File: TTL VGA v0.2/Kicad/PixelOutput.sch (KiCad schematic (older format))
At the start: 5 parts, among them U19 GAL16V8

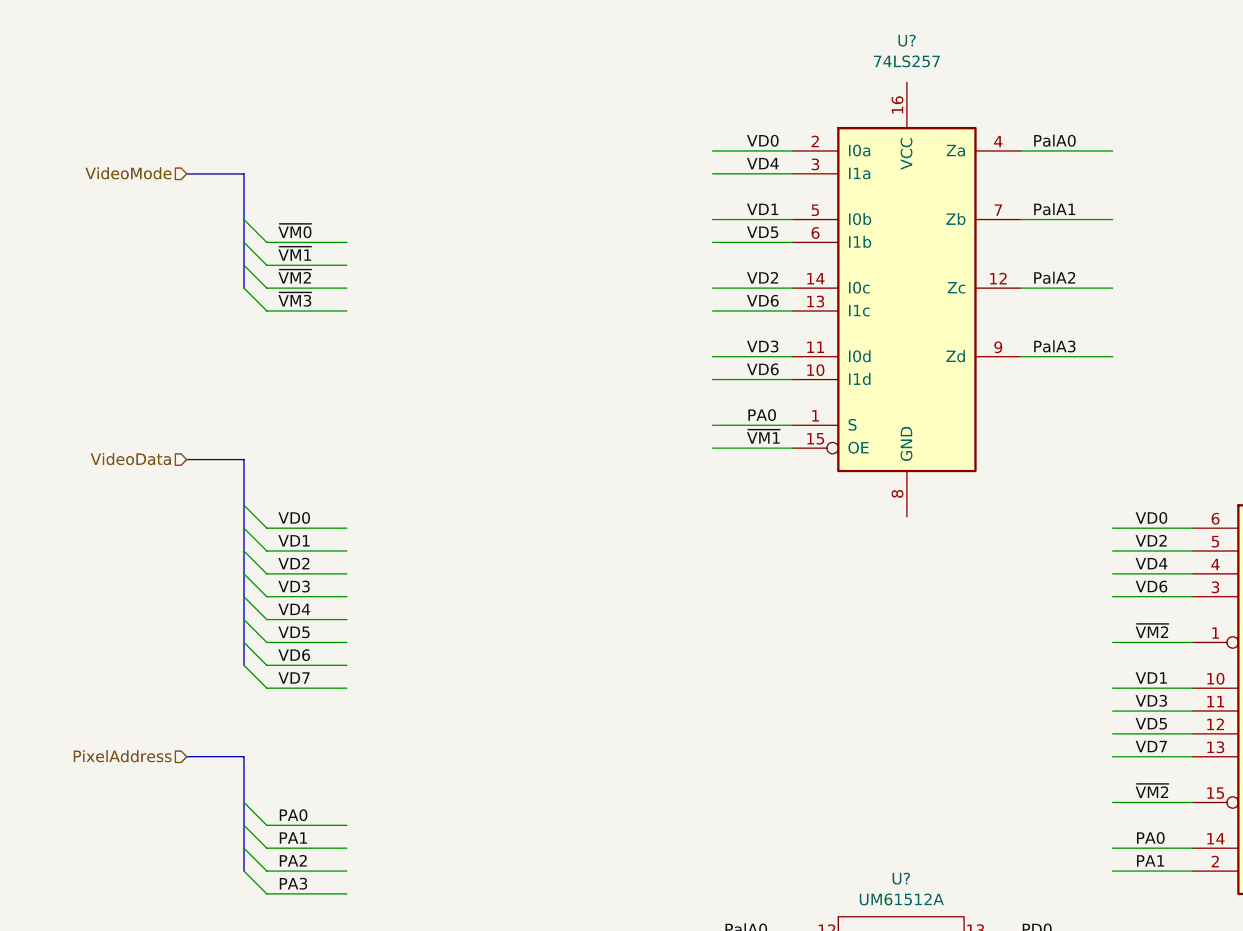
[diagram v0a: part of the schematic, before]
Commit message: video bit mux
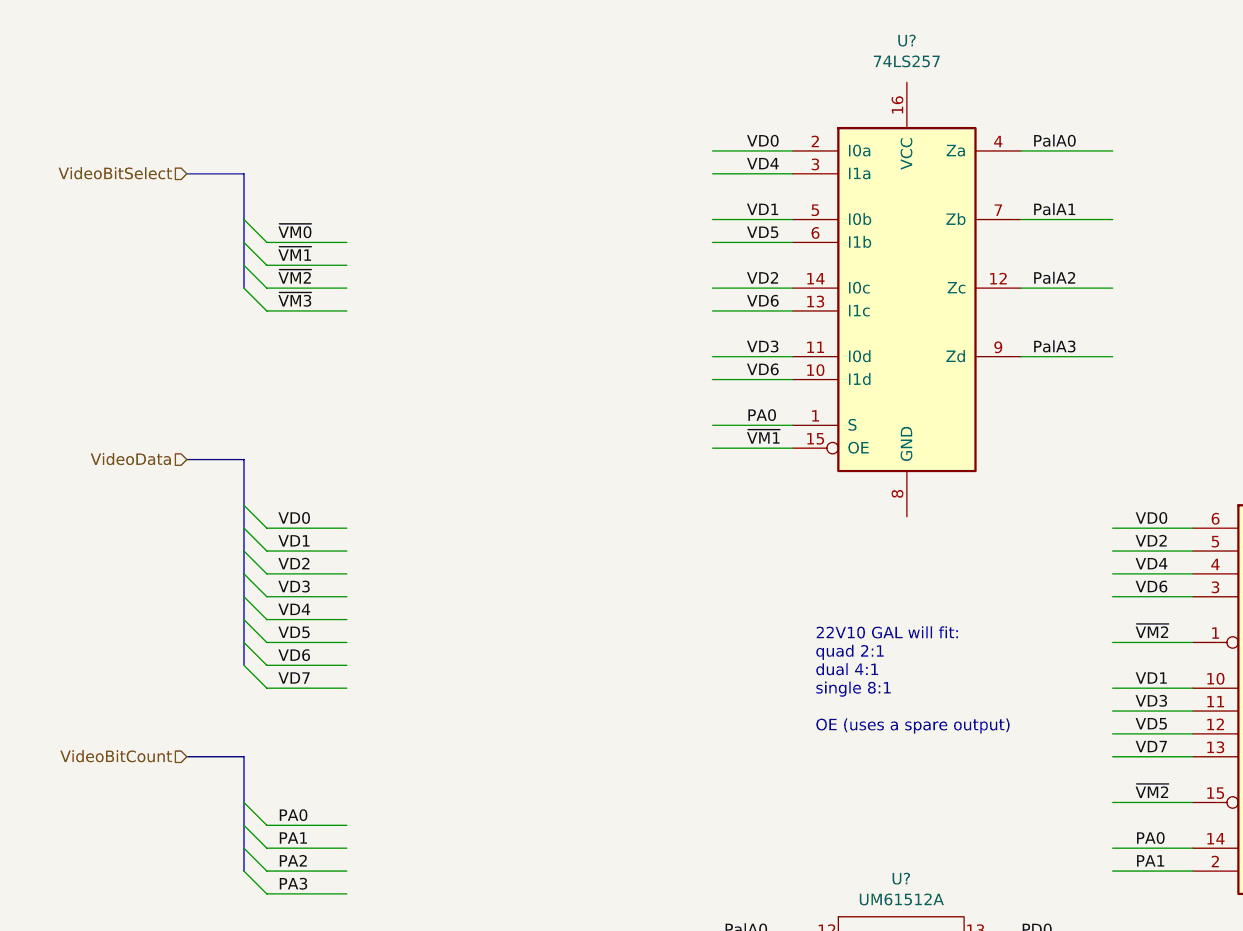
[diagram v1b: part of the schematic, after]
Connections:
- net labels added: VideoBitCount, VideoBitSelect
- net labels removed: PixelAddress, VideoMode
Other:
- note added: "22V10 GAL will fit:\nquad 2:1\ndual 4:1\nsingle 8:1\n\nOE (uses a spare output)"
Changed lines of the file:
@@
 $EndComp
 Text HLabel 1450 1650 0    50   Input ~ 0
-VideoMode
+VideoBitSelect
 Text HLabel 1450 4200 0    50   Input ~ 0
-PixelAddress
+VideoBitCount
 Text Notes 4200 7450 0    50   ~ 0
           VD0  VD1  VD2  VD3  VD4  VD5  VD6  VD7\nVM1: | PA = 0                   | PA = 1                    \nVM2: | PA = 0   | PA =1    | PA = 2    | PA = 3\nVM3: | PA0  | PA1 | PA2 | PA3 | PA4 | PA5 | PA6 | PA7\n
@@
 Wire Wire Line
 	4950 5000 5300 5000
-Wire Bus Line
-	1700 1650 1700 2150
-Wire Bus Line
-	1700 4200 1700 4700
-Wire Bus Line
-	1700 2900 1700 3800
 Wire Wire Line
 	4950 5100 5300 5100
@@
 Text Label 5100 5700 0    50   ~ 0
 PD7
+Wire Bus Line
+	1700 1650 1700 2150
+Wire Bus Line
+	1700 4200 1700 4700
+Wire Bus Line
+	1700 2900 1700 3800
+Text Notes 4200 4100 0    50   ~ 0
+22V10 GAL will fit:\nquad 2:1\ndual 4:1\nsingle 8:1\n\nOE (uses a spare output)
 $EndSCHEMATC

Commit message: update kicad
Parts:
- added U?: 74HCT574, symbol 74xx:74HCT574
- added U?: 74LS245, symbol 74xx:74LS245
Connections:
- net labels added: BD0, BD1, BD2, BD3, BD4, BD5, BD6, BD7, BusData, ColorDepthSelect, PalA10, PalA11, PalA7, PalA8, PalA9, PaletteRegStrobe, ~1bit, ~2bit, ~4bit, ~8bit, ~CDS0, ~CDS1, ~CDS2
- net labels removed: VideoBitSelect, ~VM0, ~VM1, ~VM2, ~VM3
- wire segments 99 -> 132
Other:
- note added: "8-bit color depth will bypass the Palette.\nIf we have 8-bit colors.\nIf we choose 15/16-bit colors we need to map."
- note added: "Have a Register that selects the Palette\nto switch quickly between presets.\nOnly if not 8-bit color depth.\nStobe allowed mid-frame."
- note removed: "VD0 VD1 VD2 VD3 VD4 VD5 VD6 VD7\nVM1: | PA = 0 | PA = 1 \nVM2: | PA = 0 | PA =1 | PA = 2 | PA = 3\nVM3: | PA0 | PA1 | PA2 | PA3 | PA4 | PA5 | PA6 | PA7\n"
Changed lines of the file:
@@
 Wire Wire Line
 	9800 2000 10600 2000
-Wire Wire Line
-	9800 2100 10050 2100
-Wire Wire Line
-	9800 2200 10600 2200
 Text Label 10400 1500 0    50   ~ 0
 R0
@@
 B2
 Wire Wire Line
-	10050 2100 10050 2300
-Connection ~ 10050 2100
-Wire Wire Line
-	10050 2100 10600 2100
-Wire Wire Line
 	10050 2300 10600 2300
 Text Notes 9050 950  0    50   ~ 0
@@
 $EndComp
 Text HLabel 1450 1650 0    50   Input ~ 0
-VideoBitSelect
+ColorDepthSelect
 Text HLabel 1450 4200 0    50   Input ~ 0
 VideoBitCount
-Text Notes 4200 7450 0    50   ~ 0
-          VD0  VD1  VD2  VD3  VD4  VD5  VD6  VD7\nVM1: | PA = 0                   | PA = 1                    \nVM2: | PA = 0   | PA =1    | PA = 2    | PA = 3\nVM3: | PA0  | PA1 | PA2 | PA3 | PA4 | PA5 | PA6 | PA7\n
 $Comp
 L 74xx:74LS251 U?
@@
 	7550 5800 7200 5800
 Text Label 7350 5800 0    50   ~ 0
-~VM3
+~1bit
 $Comp
 L 74xx:74LS253 U?
@@
 VD7
 Text Label 5600 3700 0    50   ~ 0
-~VM2
+~2bit
 Text Label 5600 4400 0    50   ~ 0
-~VM2
+~2bit
 Text Label 5600 4600 0    50   ~ 0
 PA0
@@
 PalA3
 Text Label 3900 2850 0    50   ~ 0
-~VM1
+~4bit
 Text Label 3900 2750 0    50   ~ 0
 PA0
@@
 Entry Wire Line
 	1700 2050 1800 2150
-Entry Wire Line
-	1700 2150 1800 2250
 Wire Bus Line
 	1700 1650 1450 1650
-Wire Wire Line
-	1800 1950 2150 1950
-Wire Wire Line
-	1800 2050 2150 2050
-Wire Wire Line
-	1800 2150 2150 2150
-Wire Wire Line
-	1800 2250 2150 2250
 Text Label 1850 1950 0    50   ~ 0
-~VM0
+~CDS0
 Text Label 1850 2050 0    50   ~ 0
-~VM1
+~CDS1
 Text Label 1850 2150 0    50   ~ 0
-~VM2
-Text Label 1850 2250 0    50   ~ 0
-~VM3
+~CDS2
 Text Notes 4350 6750 0    50   ~ 0
 Palette RAM
@@
 Text Label 5100 5700 0    50   ~ 0
 PD7
-Wire Bus Line
-	1700 1650 1700 2150
-Wire Bus Line
-	1700 4200 1700 4700
-Wire Bus Line
-	1700 2900 1700 3800
 Text Notes 4200 4100 0    50   ~ 0
 22V10 GAL will fit:\nquad 2:1\ndual 4:1\nsingle 8:1\n\nOE (uses a spare output)
+Wire Wire Line
+	4200 5700 3750 5700
+Wire Wire Line
+	4200 5800 3750 5800
+Text Label 3800 5700 0    50   ~ 0
+PalA7
+Wire Wire Line
+	4200 5900 3750 5900
+Wire Wire Line
+	4200 6000 3750 6000
+Wire Wire Line
+	4200 6100 3750 6100
+Text Notes 950  7200 0    50   ~ 0
+Have a Register that selects the Palette\nto switch quickly between presets.\nOnly if not 8-bit color depth.\nStobe allowed mid-frame.
+Text Notes 5250 6300 0    50   ~ 0
+8-bit color depth will bypass the Palette.\nIf we have 8-bit colors.\nIf we choose 15/16-bit colors we need to map.
+$Comp
+L 74xx:74HCT574 U?
+U 1 1 5EBE347D
+P 1900 6050
+F 0 "U?" H 1900 7031 50  0000 C CNN
+F 1 "74HCT574" H 1900 6940 50  0000 C CNN
+F 2 "" H 1900 6050 50  0001 C CNN
+F 3 "http://www.ti.com/lit/gpn/sn74HCT574" H 1900 6050 50  0001 C CNN
+	1    1900 6050
+	1    0    0    -1
+$EndComp
+Wire Wire Line
+	1400 5550 1050 5550
+Wire Wire Line
+	1400 5650 1050 5650
+Wire Wire Line
+	1400 5750 1050 5750
+Wire Wire Line
+	1400 5850 1050 5850
+Wire Wire Line
+	1400 5950 1050 5950
+Wire Wire Line
+	1400 6050 1050 6050
+Wire Wire Line
+	1400 6150 1050 6150
+Wire Wire Line
+	1400 6250 1050 6250
+Entry Wire Line
+	950  5450 1050 5550
+Entry Wire Line
+	950  5550 1050 5650
+Entry Wire Line
+	950  5650 1050 5750
+Entry Wire Line
+	950  5750 1050 5850
+Entry Wire Line
+	950  5850 1050 5950
+Entry Wire Line
+	950  5950 1050 6050
+Entry Wire Line
+	950  6050 1050 6150
+Entry Wire Line
+	950  6150 1050 6250
+Wire Bus Line
+	950  5350 850  5350
+Text HLabel 850  5350 0    50   Input ~ 0
+BusData
+Text HLabel 1200 6450 0    50   Input ~ 0
+PaletteRegStrobe
+Wire Wire Line
+	1200 6450 1400 6450
+Text Label 1100 5550 0    50   ~ 0
+BD0
+Text Label 1100 5650 0    50   ~ 0
+BD1
+Text Label 1100 5750 0    50   ~ 0
+BD2
+Text Label 1100 5850 0    50   ~ 0
+BD3
+Text Label 1100 5950 0    50   ~ 0
+BD4
+Text Label 1100 6050 0    50   ~ 0
+BD5
+Text Label 1100 6150 0    50   ~ 0
+BD6
+Text Label 1100 6250 0    50   ~ 0
+BD7
+Wire Wire Line
+	2400 5550 2800 5550
+Wire Wire Line
+	2400 5650 2800 5650
+Wire Wire Line
+	2400 5750 2800 5750
+Wire Wire Line
+	2400 5850 2800 5850
+Wire Wire Line
+	2400 5950 2800 5950
+Wire Wire Line
+	2400 6050 2800 6050
+Wire Wire Line
+	2400 6150 2800 6150
+Wire Wire Line
+	2400 6250 2800 6250
+Text Label 2500 5550 0    50   ~ 0
+PalA4
+Text Label 2500 5650 0    50   ~ 0
+PalA5
+Text Label 2500 5750 0    50   ~ 0
+PalA6
+Text Label 2500 5850 0    50   ~ 0
+PalA7
+Text Label 2500 5950 0    50   ~ 0
+PalA8
+Text Label 2500 6050 0    50   ~ 0
+PalA9
+Text Label 2500 6150 0    50   ~ 0
+PalA10
+Text Label 2500 6250 0    50   ~ 0
+PalA11
+Text Label 3800 5800 0    50   ~ 0
+PalA8
+Text Label 3800 5900 0    50   ~ 0
+PalA9
+Text Label 3800 6000 0    50   ~ 0
+PalA10
+Text Label 3800 6100 0    50   ~ 0
+PalA11
+$Comp
+L 74xx:74LS245 U?
+U 1 1 5EC04F82
+P 2650 3700
+F 0 "U?" H 2650 4681 50  0000 C CNN
+F 1 "74LS245" H 2650 4590 50  0000 C CNN
+F 2 "" H 2650 3700 50  0001 C CNN
+F 3 "http://www.ti.com/lit/gpn/sn74LS245" H 2650 3700 50  0001 C CNN
+	1    2650 3700
+	1    0    0    -1
+$EndComp
+Wire Wire Line
+	3150 3200 3450 3200
+Wire Wire Line
+	3150 3300 3450 3300
+Wire Wire Line
+	3150 3400 3450 3400
+Wire Wire Line
+	3150 3500 3450 3500
+Wire Wire Line
+	3150 3600 3450 3600
+Wire Wire Line
+	3150 3700 3450 3700
+Wire Wire Line
+	3150 3800 3450 3800
+Wire Wire Line
+	3150 3900 3450 3900
+Text Label 3250 3200 0    50   ~ 0
+PD0
+Text Label 3250 3300 0    50   ~ 0
+PD1
+Text Label 3250 3400 0    50   ~ 0
+PD2
+Text Label 3250 3500 0    50   ~ 0
+PD3
+Text Label 3250 3600 0    50   ~ 0
+PD4
+Text Label 3250 3700 0    50   ~ 0
+PD5
+Text Label 3250 3800 0    50   ~ 0
+PD6
+Text Label 3250 3900 0    50   ~ 0
+PD7
+Wire Wire Line
+	2150 4200 1850 4200
+Text Label 1900 4200 0    50   ~ 0
+~8bit
+Wire Wire Line
+	9800 2100 10150 2100
+Wire Wire Line
+	9800 2200 10050 2200
+Wire Wire Line
+	10050 2200 10050 2300
+Wire Wire Line
+	10600 2200 10150 2200
+Wire Wire Line
+	10150 2200 10150 2100
+Connection ~ 10150 2100
+Wire Wire Line
+	10150 2100 10600 2100
+Wire Wire Line
+	1800 1950 2650 1950
+Wire Wire Line
+	1800 2050 2650 2050
+Wire Wire Line
+	1800 2150 2650 2150
+Text Label 2450 1950 0    50   ~ 0
+~1bit
+Text Label 2450 2050 0    50   ~ 0
+~2bit
+Text Label 2450 2150 0    50   ~ 0
+~4bit
+Wire Wire Line
+	1800 2300 2650 2300
+Wire Bus Line
+	1700 1650 1700 2050
+Wire Bus Line
+	1700 4200 1700 4700
+Wire Bus Line
+	950  5350 950  6150
+Wire Bus Line
+	1700 2900 1700 3800
+Text Label 2450 2300 0    50   ~ 0
+~8bit
 $EndSCHEMATC

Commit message: Update
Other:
- note added: "22V10 GAL will fit:\nquad 2:1\ndual 4:1\nsingle 8:1\n\nOE (used a spare output)"
- note added: "8-bit RGB\n\nR (3-bits)\nG (3-bits)\nB (2-bits)"
- note added: "A Register that selects the active Palette.\nAllows the CPU to switch quickly between presets.\nOnly if not 8-bit color depth.\nStobe allowed mid-frame."
- note added: "Data from VRAM"
- note added: "Pixel-Address lines that \nselect what data bits to \nselect for the output of \neach pixel. (multiple \npixels per VRAM-Address)"
- note added: "TODO: 8-bit mode"
- note added: "TODO: RGB (9-bit) DAC"
- note added: "The output will be 'black' when \neither blank signal is active,\n"
- note added: "This module contains the color palette \nand color depth selection logic for the \nvarious video modes."
- note added: "bits per pixel"
- note removed: "22V10 GAL will fit:\nquad 2:1\ndual 4:1\nsingle 8:1\n\nOE (uses a spare output)"
- note removed: "Have a Register that selects the Palette\nto switch quickly between presets.\nOnly if not 8-bit color depth.\nStobe allowed mid-frame."
- moved on the sheet: U?
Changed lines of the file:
@@
 PD7
 Text Notes 4200 4100 0    50   ~ 0
-22V10 GAL will fit:\nquad 2:1\ndual 4:1\nsingle 8:1\n\nOE (uses a spare output)
+22V10 GAL will fit:\nquad 2:1\ndual 4:1\nsingle 8:1\n\nOE (used a spare output)
 Wire Wire Line
 	4200 5700 3750 5700
@@
 Wire Wire Line
 	4200 6100 3750 6100
-Text Notes 950  7200 0    50   ~ 0
-Have a Register that selects the Palette\nto switch quickly between presets.\nOnly if not 8-bit color depth.\nStobe allowed mid-frame.
+Text Notes 1100 7250 0    50   ~ 0
+A Register that selects the active Palette.\nAllows the CPU to switch quickly between presets.\nOnly if not 8-bit color depth.\nStobe allowed mid-frame.
 Text Notes 5250 6300 0    50   ~ 0
 8-bit color depth will bypass the Palette.\nIf we have 8-bit colors.\nIf we choose 15/16-bit colors we need to map.
@@
 L 74xx:74HCT574 U?
 U 1 1 5EBE347D
-P 1900 6050
-F 0 "U?" H 1900 7031 50  0000 C CNN
-F 1 "74HCT574" H 1900 6940 50  0000 C CNN
-F 2 "" H 1900 6050 50  0001 C CNN
-F 3 "http://www.ti.com/lit/gpn/sn74HCT574" H 1900 6050 50  0001 C CNN
-	1    1900 6050
+P 2050 6100
+F 0 "U?" H 2050 7081 50  0000 C CNN
+F 1 "74HCT574" H 2050 6990 50  0000 C CNN
+F 2 "" H 2050 6100 50  0001 C CNN
+F 3 "http://www.ti.com/lit/gpn/sn74HCT574" H 2050 6100 50  0001 C CNN
+	1    2050 6100
 	1    0    0    -1
 $EndComp
 Wire Wire Line
-	1400 5550 1050 5550
-Wire Wire Line
-	1400 5650 1050 5650
-Wire Wire Line
-	1400 5750 1050 5750
-Wire Wire Line
-	1400 5850 1050 5850
-Wire Wire Line
-	1400 5950 1050 5950
-Wire Wire Line
-	1400 6050 1050 6050
-Wire Wire Line
-	1400 6150 1050 6150
-Wire Wire Line
-	1400 6250 1050 6250
-Entry Wire Line
-	950  5450 1050 5550
-Entry Wire Line
-	950  5550 1050 5650
-Entry Wire Line
-	950  5650 1050 5750
-Entry Wire Line
-	950  5750 1050 5850
-Entry Wire Line
-	950  5850 1050 5950
-Entry Wire Line
-	950  5950 1050 6050
-Entry Wire Line
-	950  6050 1050 6150
-Entry Wire Line
-	950  6150 1050 6250
-Wire Bus Line
-	950  5350 850  5350
-Text HLabel 850  5350 0    50   Input ~ 0
+	1550 5600 1200 5600
+Wire Wire Line
+	1550 5700 1200 5700
+Wire Wire Line
+	1550 5800 1200 5800
+Wire Wire Line
+	1550 5900 1200 5900
+Wire Wire Line
+	1550 6000 1200 6000
+Wire Wire Line
+	1550 6100 1200 6100
+Wire Wire Line
+	1550 6200 1200 6200
+Wire Wire Line
+	1550 6300 1200 6300
+Entry Wire Line
+	1100 5500 1200 5600
+Entry Wire Line
+	1100 5600 1200 5700
+Entry Wire Line
+	1100 5700 1200 5800
+Entry Wire Line
+	1100 5800 1200 5900
+Entry Wire Line
+	1100 5900 1200 6000
+Entry Wire Line
+	1100 6000 1200 6100
+Entry Wire Line
+	1100 6100 1200 6200
+Entry Wire Line
+	1100 6200 1200 6300
+Wire Bus Line
+	1100 5400 1000 5400
+Text HLabel 1000 5400 0    50   Input ~ 0
 BusData
-Text HLabel 1200 6450 0    50   Input ~ 0
+Text HLabel 1350 6500 0    50   Input ~ 0
 PaletteRegStrobe
 Wire Wire Line
-	1200 6450 1400 6450
-Text Label 1100 5550 0    50   ~ 0
+	1350 6500 1550 6500
+Text Label 1250 5600 0    50   ~ 0
 BD0
-Text Label 1100 5650 0    50   ~ 0
+Text Label 1250 5700 0    50   ~ 0
 BD1
-Text Label 1100 5750 0    50   ~ 0
+Text Label 1250 5800 0    50   ~ 0
 BD2
-Text Label 1100 5850 0    50   ~ 0
+Text Label 1250 5900 0    50   ~ 0
 BD3
-Text Label 1100 5950 0    50   ~ 0
+Text Label 1250 6000 0    50   ~ 0
 BD4
-Text Label 1100 6050 0    50   ~ 0
+Text Label 1250 6100 0    50   ~ 0
 BD5
-Text Label 1100 6150 0    50   ~ 0
+Text Label 1250 6200 0    50   ~ 0
 BD6
-Text Label 1100 6250 0    50   ~ 0
+Text Label 1250 6300 0    50   ~ 0
 BD7
 Wire Wire Line
-	2400 5550 2800 5550
-Wire Wire Line
-	2400 5650 2800 5650
-Wire Wire Line
-	2400 5750 2800 5750
-Wire Wire Line
-	2400 5850 2800 5850
-Wire Wire Line
-	2400 5950 2800 5950
-Wire Wire Line
-	2400 6050 2800 6050
-Wire Wire Line
-	2400 6150 2800 6150
-Wire Wire Line
-	2400 6250 2800 6250
-Text Label 2500 5550 0    50   ~ 0
+	2550 5600 2950 5600
+Wire Wire Line
+	2550 5700 2950 5700
+Wire Wire Line
+	2550 5800 2950 5800
+Wire Wire Line
+	2550 5900 2950 5900
+Wire Wire Line
+	2550 6000 2950 6000
+Wire Wire Line
+	2550 6100 2950 6100
+Wire Wire Line
+	2550 6200 2950 6200
+Wire Wire Line
+	2550 6300 2950 6300
+Text Label 2650 5600 0    50   ~ 0
 PalA4
-Text Label 2500 5650 0    50   ~ 0
+Text Label 2650 5700 0    50   ~ 0
 PalA5
-Text Label 2500 5750 0    50   ~ 0
+Text Label 2650 5800 0    50   ~ 0
 PalA6
-Text Label 2500 5850 0    50   ~ 0
+Text Label 2650 5900 0    50   ~ 0
 PalA7
-Text Label 2500 5950 0    50   ~ 0
+Text Label 2650 6000 0    50   ~ 0
 PalA8
-Text Label 2500 6050 0    50   ~ 0
+Text Label 2650 6100 0    50   ~ 0
 PalA9
-Text Label 2500 6150 0    50   ~ 0
+Text Label 2650 6200 0    50   ~ 0
 PalA10
-Text Label 2500 6250 0    50   ~ 0
+Text Label 2650 6300 0    50   ~ 0
 PalA11
 Text Label 3800 5800 0    50   ~ 0
@@
 Wire Wire Line
 	1800 2300 2650 2300
-Wire Bus Line
-	1700 1650 1700 2050
-Wire Bus Line
-	1700 4200 1700 4700
-Wire Bus Line
-	950  5350 950  6150
-Wire Bus Line
-	1700 2900 1700 3800
 Text Label 2450 2300 0    50   ~ 0
 ~8bit
+Text Notes 850  950  0    49   ~ 0
+This module contains the color palette \nand color depth selection logic for the \nvarious video modes.
+Text Notes 9750 2850 0    49   ~ 0
+8-bit RGB\n\nR (3-bits)\nG (3-bits)\nB (2-bits)
+Text Notes 10150 1350 0    49   ~ 0
+TODO: RGB (9-bit) DAC
+Text Notes 1800 2500 0    49   ~ 0
+TODO: 8-bit mode
+Text Notes 1000 2800 0    49   ~ 0
+Data from VRAM
+Text Notes 7400 900  0    49   ~ 0
+The output will be 'black' when \neither blank signal is active,\n
+Text Notes 650  4700 0    49   ~ 0
+Pixel-Address lines that \nselect what data bits to \nselect for the output of \neach pixel. (multiple \npixels per VRAM-Address)
+Wire Bus Line
+	1700 1650 1700 2050
+Wire Bus Line
+	1700 4200 1700 4700
+Wire Bus Line
+	1100 5400 1100 6200
+Wire Bus Line
+	1700 2900 1700 3800
+Text Notes 2400 1800 0    49   ~ 0
+bits per pixel
 $EndSCHEMATC
